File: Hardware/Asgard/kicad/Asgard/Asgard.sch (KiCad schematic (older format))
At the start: 9 parts

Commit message: secret is the wash
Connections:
- net at BLUESMIRF1.1 (P1): now also BLUESMIRF1.6 (P6)
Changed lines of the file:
@@
 Wire Wire Line
 	3800 2350 3650 2350
+Wire Wire Line
+	5100 4750 5200 4750
+Wire Wire Line
+	5100 4750 5100 5250
+Wire Wire Line
+	5100 5250 5200 5250
 $EndSCHEMATC

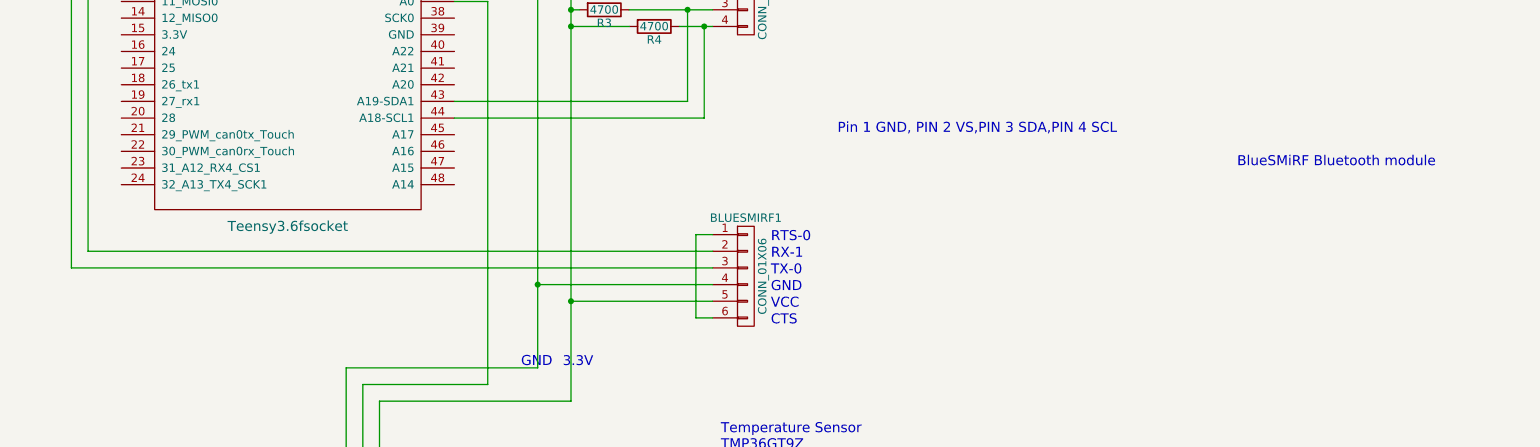
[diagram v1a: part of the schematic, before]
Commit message: Updated Schematics
Addedd indication for HC-05/HC-06 Compatibility
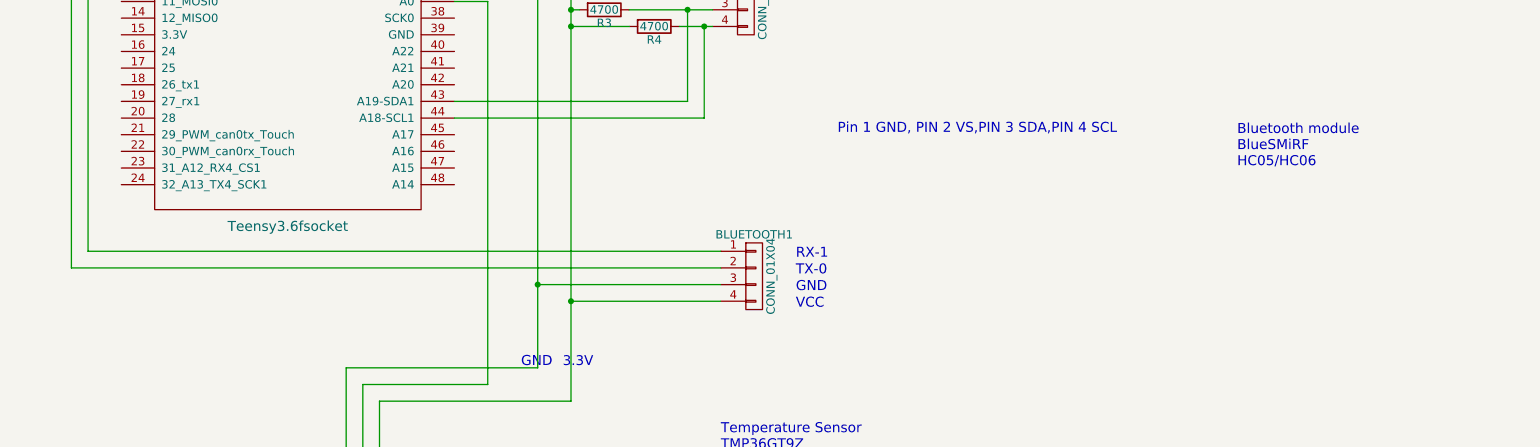
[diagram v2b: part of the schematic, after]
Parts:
- removed BLUESMIRF1: CONN_01X06, Socket_Strips:Socket_Strip_Straight_1x06_Pitch2.54mm, symbol CONN_01X06
- added BLUETOOTH1: CONN_01X04, Socket_Strips:Socket_Strip_Straight_1x04_Pitch2.54mm, symbol CONN_01X04
- ABSP1, DELTAP1: footprint Socket_Strips:Socket_Strip_Angled_1x04_Pitch2.54mm -> Socket_Strips:Socket_Strip_Straight_1x04_Pitch2.54mm
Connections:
- net +3V3: now also BLUETOOTH1.4 (P4)
- net GND: now also BLUETOOTH1.3 (P3)
- net at TEENSYV3.6.3 (1_TX1_MISO1_Touch): now also BLUETOOTH1.1 (P1)
- net at TEENSYV3.6.2 (0_RX1_MOSI1_Touch): now also BLUETOOTH1.2 (P2)
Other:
- note added: "Bluetooth module\nBlueSMiRF \nHC05/HC06\n"
- note removed: "BlueSMiRF Bluetooth module"
- note removed: "CTS"
- note removed: "RTS-0"

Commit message: Fiddling with packages
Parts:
- R1, R2, R3, R4: footprint Resistors_SMD:R_1206 -> Resistors_THT:R_Axial_DIN0204_L3.6mm_D1.6mm_P5.08mm_Horizontal
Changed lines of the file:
@@
 F 0 "R1" V 4630 2300 50  0000 C CNN
 F 1 "4700" V 4550 2300 50  0000 C CNN
-F 2 "Resistors_SMD:R_1206" V 4480 2300 50  0001 C CNN
+F 2 "Resistors_THT:R_Axial_DIN0204_L3.6mm_D1.6mm_P5.08mm_Horizontal" V 4480 2300 50  0001 C CNN
 F 3 "" H 4550 2300 50  0001 C CNN
 	1    4550 2300
@@
 F 0 "R2" V 4930 2400 50  0000 C CNN
 F 1 "4700" V 4850 2400 50  0000 C CNN
-F 2 "Resistors_SMD:R_1206" V 4780 2400 50  0001 C CNN
+F 2 "Resistors_THT:R_Axial_DIN0204_L3.6mm_D1.6mm_P5.08mm_Horizontal" V 4780 2400 50  0001 C CNN
 F 3 "" H 4850 2400 50  0001 C CNN
 	1    4850 2400
@@
 F 0 "R3" V 4630 3400 50  0000 C CNN
 F 1 "4700" V 4550 3400 50  0000 C CNN
-F 2 "Resistors_SMD:R_1206" V 4480 3400 50  0001 C CNN
+F 2 "Resistors_THT:R_Axial_DIN0204_L3.6mm_D1.6mm_P5.08mm_Horizontal" V 4480 3400 50  0001 C CNN
 F 3 "" H 4550 3400 50  0001 C CNN
 	1    4550 3400
@@
 F 0 "R4" V 4930 3500 50  0000 C CNN
 F 1 "4700" V 4850 3500 50  0000 C CNN
-F 2 "Resistors_SMD:R_1206" V 4780 3500 50  0001 C CNN
+F 2 "Resistors_THT:R_Axial_DIN0204_L3.6mm_D1.6mm_P5.08mm_Horizontal" V 4780 3500 50  0001 C CNN
 F 3 "" H 4850 3500 50  0001 C CNN
 	1    4850 3500

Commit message: Schematics update
GPIO connector is hard to place
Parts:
- added GPIO1: CONN_01X03, Connect:PINHEAD1-3, symbol CONN_01X03
- OAT1: footprint Pin_Headers:Pin_Header_Angled_1x03_Pitch2.54mm -> Connect:PINHEAD1-3
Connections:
- net GND: now also GPIO1.1 (P1)
- net at TEENSYV3.6.47 (A15): now also GPIO1.2 (P2)
- net at TEENSYV3.6.48 (A14): now also GPIO1.3 (P3)
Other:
- note added: "GPIO"
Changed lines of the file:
@@
 $Bitmap
 Pos 7250 6800
-Scale 1,000000
+Scale 1.000000
 Data
 89 50 4E 47 0D 0A 1A 0A 00 00 00 0D 49 48 44 52 00 00 00 80 00 00 00 80 08 06 00 00 00 C3 3E 61
@@
 $Bitmap
 Pos 7050 5000
-Scale 1,000000
+Scale 1.000000
 Data
 89 50 4E 47 0D 0A 1A 0A 00 00 00 0D 49 48 44 52 00 00 02 58 00 00 02 58 08 02 00 00 00 31 04 0F
@@
 $Bitmap
 Pos 6800 3400
-Scale 1,000000
+Scale 1.000000
 Data
 89 50 4E 47 0D 0A 1A 0A 00 00 00 0D 49 48 44 52 00 00 02 23 00 00 01 87 08 02 00 00 00 ED 2D C5
@@
 $Bitmap
 Pos 6800 2000
-Scale 1,000000
+Scale 1.000000
 Data
 89 50 4E 47 0D 0A 1A 0A 00 00 00 0D 49 48 44 52 00 00 02 33 00 00 01 A2 08 02 00 00 00 9D E2 D0
@@
 	1    0    0    -1
 $EndComp
-Wire Wire Line
-	4350 1850 4350 5750
-Wire Wire Line
-	4700 2400 4350 2400
-Connection ~ 4350 2400
-Wire Wire Line
-	4400 2300 4350 2300
-Connection ~ 4350 2300
-Wire Wire Line
-	5000 2400 5200 2400
-Wire Wire Line
-	4700 2300 5200 2300
-Wire Wire Line
-	4400 3400 4350 3400
-Connection ~ 4350 3400
-Wire Wire Line
-	4700 3500 4350 3500
-Connection ~ 4350 3500
-Wire Wire Line
-	4700 3400 5200 3400
-Wire Wire Line
-	5000 3500 5200 3500
-Wire Wire Line
-	4150 1600 4150 5550
-Wire Wire Line
-	3650 2950 5150 2950
-Wire Wire Line
-	5150 2950 5150 2300
-Connection ~ 5150 2300
-Wire Wire Line
-	3650 2850 5050 2850
-Wire Wire Line
-	5050 2850 5050 2400
-Connection ~ 5050 2400
-Wire Wire Line
-	5200 2100 4150 2100
-Connection ~ 4150 2100
-Wire Wire Line
-	5200 3200 4150 3200
-Connection ~ 4150 3200
-Wire Wire Line
-	5200 2200 4350 2200
-Connection ~ 4350 2200
-Wire Wire Line
-	5200 3300 4350 3300
-Connection ~ 4350 3300
-Wire Wire Line
-	3650 3950 5050 3950
-Wire Wire Line
-	5050 3950 5050 3400
-Connection ~ 5050 3400
-Wire Wire Line
-	3650 4050 5150 4050
-Wire Wire Line
-	5150 4050 5150 3500
-Connection ~ 5150 3500
-Wire Wire Line
-	1450 4850 5250 4850
-Wire Wire Line
-	1450 4850 1450 2350
-Wire Wire Line
-	1450 2350 1650 2350
-Wire Wire Line
-	1350 4950 5250 4950
-Wire Wire Line
-	1350 4950 1350 2250
-Wire Wire Line
-	1350 2250 1650 2250
-Wire Wire Line
-	4150 5050 5250 5050
-Connection ~ 4150 5050
-Wire Wire Line
-	4350 5150 5250 5150
-Connection ~ 4350 5150
 Text Notes 8000 7000 0    60   ~ 0
 www.basicairdata.eu
-Wire Wire Line
-	4150 1900 1550 1900
-Wire Wire Line
-	1550 1900 1550 2150
-Wire Wire Line
-	1550 2150 1650 2150
-Connection ~ 4150 1900
-Wire Wire Line
-	3800 2000 3800 2350
-Wire Wire Line
-	3800 2000 4350 2000
-Connection ~ 4350 2000
 Text Notes 5250 6050 0    60   ~ 0
 Temperature Sensor\nTMP36GT9Z
@@
 F 0 "OAT1" H 3100 6550 50  0000 C CNN
 F 1 "CONN_01X03" V 3200 6350 50  0000 C CNN
-F 2 "Pin_Headers:Pin_Header_Angled_1x03_Pitch2.54mm" H 3100 6350 50  0001 C CNN
+F 2 "Connect:PINHEAD1-3" H 3100 6350 50  0001 C CNN
 F 3 "" H 3100 6350 50  0001 C CNN
 	1    3100 6350
@@
 $Bitmap
 Pos 4300 6300
-Scale 1,000000
+Scale 1.000000
 Data
 89 50 4E 47 0D 0A 1A 0A 00 00 00 0D 49 48 44 52 00 00 02 34 00 00 01 2F 08 02 00 00 00 DD 10 CC
@@
 Text Notes 4050 5550 0    60   ~ 0
 GND
-Wire Wire Line
-	3200 6150 3200 5750
-Wire Wire Line
-	3200 5750 4350 5750
-Wire Wire Line
-	3100 6150 3100 5650
-Wire Wire Line
-	3100 5650 3850 5650
-Wire Wire Line
-	3850 5650 3850 3350
-Wire Wire Line
-	3850 3350 3650 3350
-Wire Wire Line
-	3000 6150 3000 5550
-Wire Wire Line
-	3000 5550 4150 5550
 $Comp
 L GND #PWR01
@@
 	1    0    0    -1
 $EndComp
-Wire Wire Line
-	4150 1600 3900 1600
-Wire Wire Line
-	3900 1600 3900 1650
 $Comp
 L +3.3V #PWR02
@@
 	1    0    0    -1
 $EndComp
-Wire Wire Line
-	3800 2350 3650 2350
 $Bitmap
 Pos 9550 5400
-Scale 1,000000
+Scale 1.000000
 Data
 89 50 4E 47 0D 0A 1A 0A 00 00 00 0D 49 48 44 52 00 00 02 EE 00 00 02 32 08 02 00 00 00 1B 83 D8
@@
 	1    0    0    -1
 $EndComp
+$Comp
+L CONN_01X03 GPIO1
+U 1 1 59244C9A
+P 2000 6350
+F 0 "GPIO1" H 2000 6550 50  0000 C CNN
+F 1 "CONN_01X03" V 2100 6350 50  0000 C CNN
+F 2 "Connect:PINHEAD1-3" H 2000 6350 50  0001 C CNN
+F 3 "" H 2000 6350 50  0001 C CNN
+	1    2000 6350
+	0    1    1    0
+$EndComp
+Text Notes 1250 6050 0    60   ~ 0
+GPIO
+Wire Wire Line
+	4350 1850 4350 5750
+Wire Wire Line
+	4700 2400 4350 2400
+Connection ~ 4350 2400
+Wire Wire Line
+	4400 2300 4350 2300
+Connection ~ 4350 2300
+Wire Wire Line
+	5000 2400 5200 2400
+Wire Wire Line
+	4700 2300 5200 2300
+Wire Wire Line
+	4400 3400 4350 3400
+Connection ~ 4350 3400
+Wire Wire Line
+	4700 3500 4350 3500
+Connection ~ 4350 3500
+Wire Wire Line
+	4700 3400 5200 3400
+Wire Wire Line
+	5000 3500 5200 3500
+Wire Wire Line
+	4150 1600 4150 5550
+Wire Wire Line
+	3650 2950 5150 2950
+Wire Wire Line
+	5150 2950 5150 2300
+Connection ~ 5150 2300
+Wire Wire Line
+	3650 2850 5050 2850
+Wire Wire Line
+	5050 2850 5050 2400
+Connection ~ 5050 2400
+Wire Wire Line
+	5200 2100 4150 2100
+Connection ~ 4150 2100
+Wire Wire Line
+	5200 3200 4150 3200
+Connection ~ 4150 3200
+Wire Wire Line
+	5200 2200 4350 2200
+Connection ~ 4350 2200
+Wire Wire Line
+	5200 3300 4350 3300
+Connection ~ 4350 3300
+Wire Wire Line
+	3650 3950 5050 3950
+Wire Wire Line
+	5050 3950 5050 3400
+Connection ~ 5050 3400
+Wire Wire Line
+	3650 4050 5150 4050
+Wire Wire Line
+	5150 4050 5150 3500
+Connection ~ 5150 3500
+Wire Wire Line
+	1450 4850 5250 4850
+Wire Wire Line
+	1450 4850 1450 2350
+Wire Wire Line
+	1450 2350 1650 2350
+Wire Wire Line
+	1350 4950 5250 4950
+Wire Wire Line
+	1350 4950 1350 2250
+Wire Wire Line
+	1350 2250 1650 2250
+Wire Wire Line
+	4150 5050 5250 5050
+Connection ~ 4150 5050
+Wire Wire Line
+	4350 5150 5250 5150
+Connection ~ 4350 5150
+Wire Wire Line
+	4150 1900 1550 1900
+Wire Wire Line
+	1550 1900 1550 2150
+Wire Wire Line
+	1550 2150 1650 2150
+Connection ~ 4150 1900
+Wire Wire Line
+	3800 2000 3800 2350
+Wire Wire Line
+	3800 2000 4350 2000
+Connection ~ 4350 2000
+Wire Wire Line
+	3200 6150 3200 5750
+Wire Wire Line
+	3200 5750 4350 5750
+Wire Wire Line
+	3100 6150 3100 5650
+Wire Wire Line
+	3100 5650 4000 5650
+Wire Wire Line
+	4000 5650 4000 3350
+Wire Wire Line
+	4000 3350 3650 3350
+Wire Wire Line
+	3000 6150 3000 5550
+Wire Wire Line
+	3000 5550 4150 5550
+Wire Wire Line
+	4150 1600 3900 1600
+Wire Wire Line
+	3900 1600 3900 1650
+Wire Wire Line
+	3800 2350 3650 2350
+Wire Wire Line
+	2100 6150 2100 6000
+Wire Wire Line
+	2100 6000 3000 6000
+Connection ~ 3000 6000
+Wire Wire Line
+	1900 5350 1900 6150
+Wire Wire Line
+	3650 4450 3650 5350
+Wire Wire Line
+	3650 5350 1900 5350
+Wire Wire Line
+	3650 4350 3750 4350
+Wire Wire Line
+	3750 4350 3750 5450
+Wire Wire Line
+	3750 5450 2000 5450
+Wire Wire Line
+	2000 5450 2000 6150
 $EndSCHEMATC

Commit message: PCB Rel 1
First Release of PCB
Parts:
- removed GPIO1: CONN_01X03, Connect:PINHEAD1-3, symbol CONN_01X03
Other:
- note removed: "GPIO"
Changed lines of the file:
@@
 $Bitmap
 Pos 7250 6800
-Scale 1.000000
+Scale 1,000000
 Data
 89 50 4E 47 0D 0A 1A 0A 00 00 00 0D 49 48 44 52 00 00 00 80 00 00 00 80 08 06 00 00 00 C3 3E 61
@@
 $Bitmap
 Pos 7050 5000
-Scale 1.000000
+Scale 1,000000
 Data
 89 50 4E 47 0D 0A 1A 0A 00 00 00 0D 49 48 44 52 00 00 02 58 00 00 02 58 08 02 00 00 00 31 04 0F
@@
 $Bitmap
 Pos 6800 3400
-Scale 1.000000
+Scale 1,000000
 Data
 89 50 4E 47 0D 0A 1A 0A 00 00 00 0D 49 48 44 52 00 00 02 23 00 00 01 87 08 02 00 00 00 ED 2D C5
@@
 $Bitmap
 Pos 6800 2000
-Scale 1.000000
+Scale 1,000000
 Data
 89 50 4E 47 0D 0A 1A 0A 00 00 00 0D 49 48 44 52 00 00 02 33 00 00 01 A2 08 02 00 00 00 9D E2 D0
@@
 $Bitmap
 Pos 4300 6300
-Scale 1.000000
+Scale 1,000000
 Data
 89 50 4E 47 0D 0A 1A 0A 00 00 00 0D 49 48 44 52 00 00 02 34 00 00 01 2F 08 02 00 00 00 DD 10 CC
@@
 GND
 $Comp
-L GND #PWR01
+L GND #PWR1
 U 1 1 58DA5935
 P 3900 1650
-F 0 "#PWR01" H 3900 1400 50  0001 C CNN
+F 0 "#PWR1" H 3900 1400 50  0001 C CNN
 F 1 "GND" H 3900 1500 50  0000 C CNN
 F 2 "" H 3900 1650 50  0001 C CNN
@@
 $EndComp
 $Comp
-L +3.3V #PWR02
+L +3.3V #PWR2
 U 1 1 58DA5ABD
 P 4350 1850
-F 0 "#PWR02" H 4350 1700 50  0001 C CNN
+F 0 "#PWR2" H 4350 1700 50  0001 C CNN
 F 1 "+3.3V" H 4350 1990 50  0000 C CNN
 F 2 "" H 4350 1850 50  0001 C CNN
@@
 $Bitmap
 Pos 9550 5400
-Scale 1.000000
+Scale 1,000000
 Data
 89 50 4E 47 0D 0A 1A 0A 00 00 00 0D 49 48 44 52 00 00 02 EE 00 00 02 32 08 02 00 00 00 1B 83 D8
@@
 	1    0    0    -1
 $EndComp
-$Comp
-L CONN_01X03 GPIO1
-U 1 1 59244C9A
-P 2000 6350
-F 0 "GPIO1" H 2000 6550 50  0000 C CNN
-F 1 "CONN_01X03" V 2100 6350 50  0000 C CNN
-F 2 "Connect:PINHEAD1-3" H 2000 6350 50  0001 C CNN
-F 3 "" H 2000 6350 50  0001 C CNN
-	1    2000 6350
-	0    1    1    0
-$EndComp
-Text Notes 1250 6050 0    60   ~ 0
-GPIO
 Wire Wire Line
 	4350 1850 4350 5750
@@
 Wire Wire Line
 	3800 2350 3650 2350
-Wire Wire Line
-	2100 6150 2100 6000
-Wire Wire Line
-	2100 6000 3000 6000
-Connection ~ 3000 6000
-Wire Wire Line
-	1900 5350 1900 6150
-Wire Wire Line
-	3650 4450 3650 5350
-Wire Wire Line
-	3650 5350 1900 5350
-Wire Wire Line
-	3650 4350 3750 4350
-Wire Wire Line
-	3750 4350 3750 5450
-Wire Wire Line
-	3750 5450 2000 5450
-Wire Wire Line
-	2000 5450 2000 6150
 $EndSCHEMATC

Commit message: PCB proposal
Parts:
- added GPIO1: CONN_01X03, Connect:PINHEAD1-3, symbol CONN_01X03
- R1, R2, R3, R4: footprint Resistors_THT:R_Axial_DIN0204_L3.6mm_D1.6mm_P5.08mm_Horizontal -> Resistors_ThroughHole:R_Axial_DIN0204_L3.6mm_D1.6mm_P1.90mm_Vertical
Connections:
- net GND: now also GPIO1.3 (P3)
- net at TEENSYV3.6.47 (A15): now also GPIO1.1 (P1)
- net at TEENSYV3.6.48 (A14): now also GPIO1.2 (P2)
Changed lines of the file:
@@
 $Bitmap
 Pos 7250 6800
-Scale 1,000000
+Scale 1.000000
 Data
 89 50 4E 47 0D 0A 1A 0A 00 00 00 0D 49 48 44 52 00 00 00 80 00 00 00 80 08 06 00 00 00 C3 3E 61
@@
 $Bitmap
 Pos 7050 5000
-Scale 1,000000
+Scale 1.000000
 Data
 89 50 4E 47 0D 0A 1A 0A 00 00 00 0D 49 48 44 52 00 00 02 58 00 00 02 58 08 02 00 00 00 31 04 0F
@@
 $Bitmap
 Pos 6800 3400
-Scale 1,000000
+Scale 1.000000
 Data
 89 50 4E 47 0D 0A 1A 0A 00 00 00 0D 49 48 44 52 00 00 02 23 00 00 01 87 08 02 00 00 00 ED 2D C5
@@
 $Bitmap
 Pos 6800 2000
-Scale 1,000000
+Scale 1.000000
 Data
 89 50 4E 47 0D 0A 1A 0A 00 00 00 0D 49 48 44 52 00 00 02 33 00 00 01 A2 08 02 00 00 00 9D E2 D0
@@
 F 0 "R1" V 4630 2300 50  0000 C CNN
 F 1 "4700" V 4550 2300 50  0000 C CNN
-F 2 "Resistors_THT:R_Axial_DIN0204_L3.6mm_D1.6mm_P5.08mm_Horizontal" V 4480 2300 50  0001 C CNN
+F 2 "Resistors_ThroughHole:R_Axial_DIN0204_L3.6mm_D1.6mm_P1.90mm_Vertical" V 4480 2300 50  0001 C CNN
 F 3 "" H 4550 2300 50  0001 C CNN
 	1    4550 2300
@@
 F 0 "R2" V 4930 2400 50  0000 C CNN
 F 1 "4700" V 4850 2400 50  0000 C CNN
-F 2 "Resistors_THT:R_Axial_DIN0204_L3.6mm_D1.6mm_P5.08mm_Horizontal" V 4780 2400 50  0001 C CNN
+F 2 "Resistors_ThroughHole:R_Axial_DIN0204_L3.6mm_D1.6mm_P1.90mm_Vertical" V 4780 2400 50  0001 C CNN
 F 3 "" H 4850 2400 50  0001 C CNN
 	1    4850 2400
@@
 F 0 "R3" V 4630 3400 50  0000 C CNN
 F 1 "4700" V 4550 3400 50  0000 C CNN
-F 2 "Resistors_THT:R_Axial_DIN0204_L3.6mm_D1.6mm_P5.08mm_Horizontal" V 4480 3400 50  0001 C CNN
+F 2 "Resistors_ThroughHole:R_Axial_DIN0204_L3.6mm_D1.6mm_P1.90mm_Vertical" V 4480 3400 50  0001 C CNN
 F 3 "" H 4550 3400 50  0001 C CNN
 	1    4550 3400
@@
 F 0 "R4" V 4930 3500 50  0000 C CNN
 F 1 "4700" V 4850 3500 50  0000 C CNN
-F 2 "Resistors_THT:R_Axial_DIN0204_L3.6mm_D1.6mm_P5.08mm_Horizontal" V 4780 3500 50  0001 C CNN
+F 2 "Resistors_ThroughHole:R_Axial_DIN0204_L3.6mm_D1.6mm_P1.90mm_Vertical" V 4780 3500 50  0001 C CNN
 F 3 "" H 4850 3500 50  0001 C CNN
 	1    4850 3500
@@
 $Bitmap
 Pos 4300 6300
-Scale 1,000000
+Scale 1.000000
 Data
 89 50 4E 47 0D 0A 1A 0A 00 00 00 0D 49 48 44 52 00 00 02 34 00 00 01 2F 08 02 00 00 00 DD 10 CC
@@
 GND
 $Comp
-L GND #PWR1
+L GND #PWR01
 U 1 1 58DA5935
 P 3900 1650
-F 0 "#PWR1" H 3900 1400 50  0001 C CNN
+F 0 "#PWR01" H 3900 1400 50  0001 C CNN
 F 1 "GND" H 3900 1500 50  0000 C CNN
 F 2 "" H 3900 1650 50  0001 C CNN
@@
 $EndComp
 $Comp
-L +3.3V #PWR2
+L +3.3V #PWR02
 U 1 1 58DA5ABD
 P 4350 1850
-F 0 "#PWR2" H 4350 1700 50  0001 C CNN
+F 0 "#PWR02" H 4350 1700 50  0001 C CNN
 F 1 "+3.3V" H 4350 1990 50  0000 C CNN
 F 2 "" H 4350 1850 50  0001 C CNN
@@
 $Bitmap
 Pos 9550 5400
-Scale 1,000000
+Scale 1.000000
 Data
 89 50 4E 47 0D 0A 1A 0A 00 00 00 0D 49 48 44 52 00 00 02 EE 00 00 02 32 08 02 00 00 00 1B 83 D8
@@
 Wire Wire Line
 	3800 2350 3650 2350
+$Comp
+L CONN_01X03 GPIO1
+U 1 1 59259417
+P 2300 6350
+F 0 "GPIO1" H 2300 6550 50  0000 C CNN
+F 1 "CONN_01X03" V 2400 6350 50  0000 C CNN
+F 2 "Connect:PINHEAD1-3" H 2300 6350 50  0001 C CNN
+F 3 "" H 2300 6350 50  0001 C CNN
+	1    2300 6350
+	0    1    1    0
+$EndComp
+Wire Wire Line
+	2200 6150 2200 6000
+Wire Wire Line
+	2200 6000 3000 6000
+Wire Wire Line
+	3000 6000 3000 5950
+Connection ~ 3000 5950
+Wire Wire Line
+	3800 5200 2300 5200
+Wire Wire Line
+	2300 5200 2300 6150
+Wire Wire Line
+	2400 6150 2400 5350
+Wire Wire Line
+	2400 5350 3900 5350
+Wire Wire Line
+	3800 5200 3800 4450
+Wire Wire Line
+	3800 4450 3650 4450
+Wire Wire Line
+	3650 4350 3900 4350
+Wire Wire Line
+	3900 4350 3900 5350
 $EndSCHEMATC
